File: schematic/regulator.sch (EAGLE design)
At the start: 24 parts, among them J1 COMM, J2 STOP_LIGHT, J3 ON/OFF, J4 IN, J5 DRIVER, Q1 NMOSFETSOT23, Q2 NMOSFETSOT23, Q3 NMOSFETSOT23

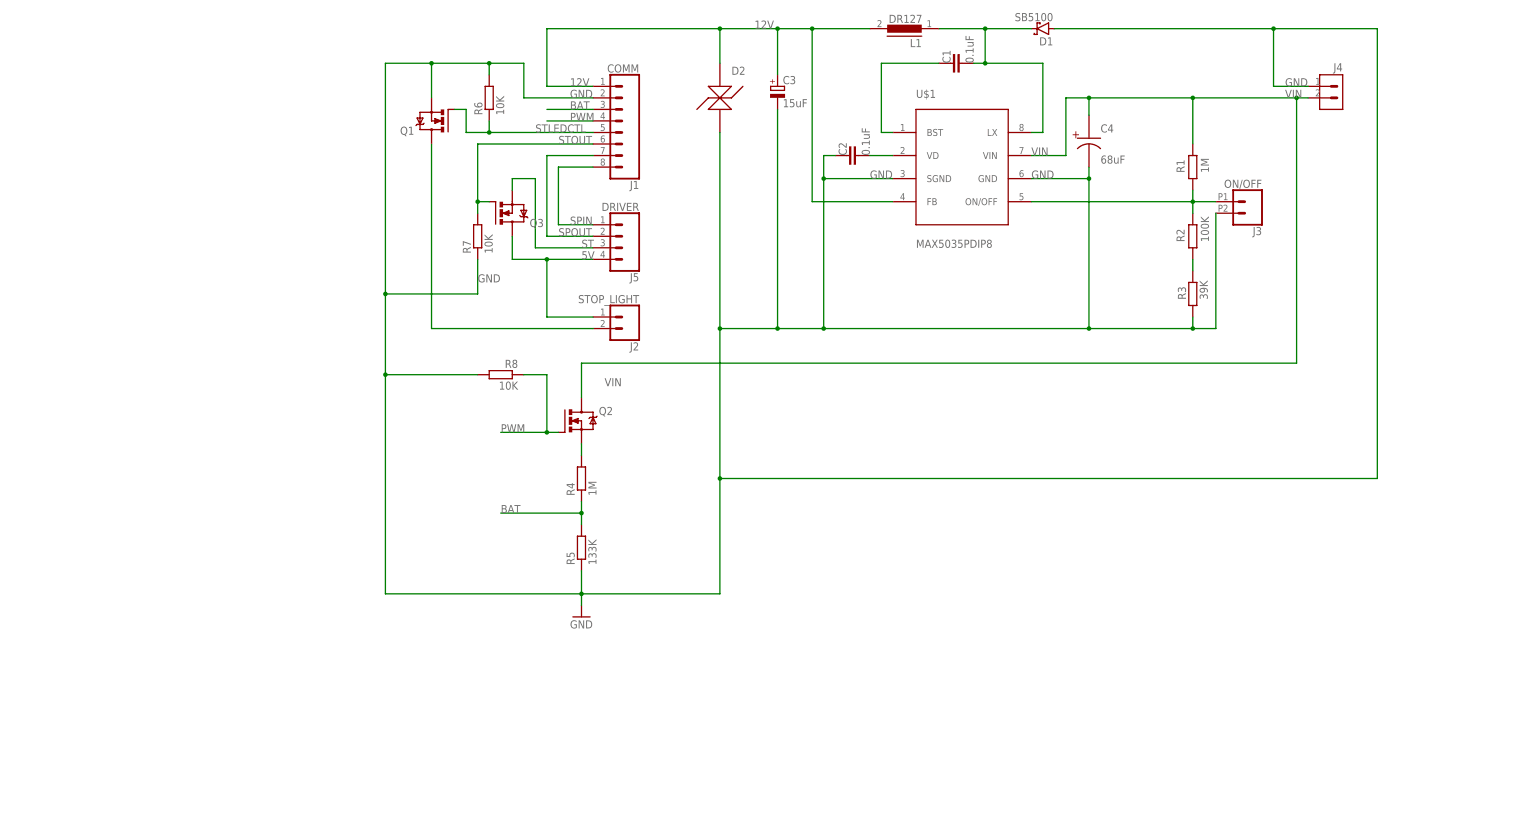
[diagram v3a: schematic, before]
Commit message: Rearrange elements in regulator schematics
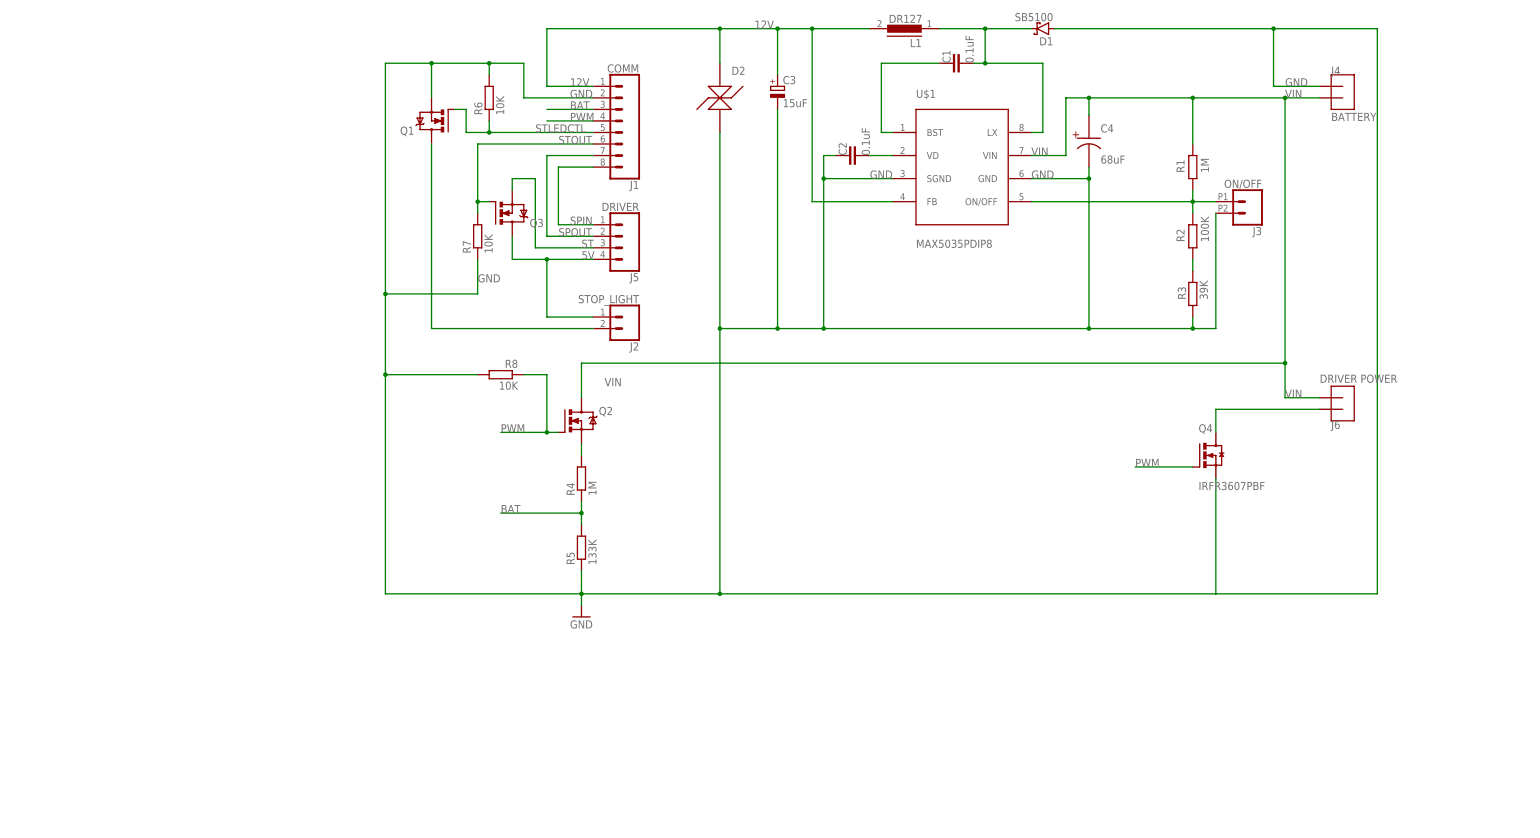
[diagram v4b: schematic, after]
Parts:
- added J6: DRIVER POWER, eScooter:XT60
- added Q4: IRFR3607PBF, Transistor:FQD13N06LTM
- J4: value IN -> BATTERY; device Connectors:B2P-VH(LF)(SN) -> eScooter:XT60
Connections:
- new net P$1: J6.P$1, Q4.D
- net GND: now also J4.P$1, Q4.S; no longer J4.1
- net PWM: now also Q4.G
- net VIN: now also J4.P$2, J6.P$2; no longer J4.2
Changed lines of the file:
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@@
 </classes>
 <parts>
-<part name="J4" library="Connectors" library_urn="urn:adsk.eagle:library:14555660" deviceset="B2P-VH(LF)(SN)" device="" package3d_urn="urn:adsk.eagle:package:10989917/2" value="IN"/>
 <part name="C1" library="Capacitor" library_urn="urn:adsk.eagle:library:16290819" deviceset="C" device="CHIP-1206(3216-METRIC)" package3d_urn="urn:adsk.eagle:package:16290893/2" technology="_" value="0.1uF"/>
 <part name="D1" library="Diodes" library_urn="urn:adsk.eagle:library:11396254" deviceset="MBR360G" device="" package3d_urn="urn:adsk.eagle:package:10898389/2" value="SB5100"/>
@@
 <part name="C4" library="eScooter" deviceset="C" device="PANASONIC_H13" package3d_urn="urn:adsk.eagle:package:21812541/1" value="68uF"/>
 <part name="U$1" library="eScooter" deviceset="MAX5035" device="PDIP8" package3d_urn="urn:adsk.eagle:package:22059831/1"/>
+<part name="J4" library="eScooter" deviceset="XT60" device="" value="BATTERY"/>
+<part name="J6" library="eScooter" deviceset="XT60" device="" value="DRIVER POWER"/>
+<part name="Q4" library="Transistor" library_urn="urn:adsk.eagle:library:14522416" deviceset="FQD13N06LTM" device="" package3d_urn="urn:adsk.eagle:package:10893256/5" value="IRFR3607PBF"/>
 </parts>
 <sheets>
@@
 </plain>
 <instances>
-<instance part="J4" gate="G$1" x="213.36" y="116.84" smashed="yes" rot="MR0">
-<attribute name="NAME" x="215.9" y="122.682" size="1.778" layer="95" rot="MR0"/>
-</instance>
 <instance part="C1" gate="G$1" x="129.54" y="124.46" smashed="yes" rot="R90">
 <attribute name="NAME" x="129.54" y="124.46" size="1.778" layer="95" rot="R90"/>
@@
 <attribute name="NAME" x="121.92" y="116.84" size="1.778" layer="95"/>
 <attribute name="VALUE" x="121.92" y="83.82" size="1.778" layer="96"/>
+</instance>
+<instance part="J4" gate="G$1" x="215.9" y="114.3" smashed="yes">
+<attribute name="NAME" x="213.36" y="121.92" size="1.778" layer="95"/>
+<attribute name="VALUE" x="213.36" y="111.76" size="1.778" layer="96"/>
+</instance>
+<instance part="J6" gate="G$1" x="215.9" y="53.34" smashed="yes" rot="MR180">
+<attribute name="NAME" x="213.36" y="45.72" size="1.778" layer="95" rot="MR180"/>
+<attribute name="VALUE" x="210.82" y="55.88" size="1.778" layer="96" rot="MR180"/>
+</instance>
+<instance part="Q4" gate="G$1" x="185.42" y="38.1" smashed="yes">
+<attribute name="NAME" x="184.15" y="43.18" size="1.778" layer="95"/>
+<attribute name="VALUE" x="184.15" y="30.48" size="1.778" layer="96"/>
 </instance>
 </instances>
@@
 <wire x1="182.88" y1="68.58" x2="182.88" y2="66.04" width="0.1524" layer="91"/>
 <wire x1="182.88" y1="66.04" x2="160.02" y2="66.04" width="0.1524" layer="91"/>
-<pinref part="J4" gate="G$1" pin="1"/>
 <junction x="182.88" y="66.04"/>
 <pinref part="C3" gate="G$1" pin="-"/>
@@
 <junction x="91.44" y="66.04"/>
 <wire x1="48.26" y1="7.62" x2="78.74" y2="7.62" width="0.1524" layer="91"/>
-<wire x1="78.74" y1="7.62" x2="78.74" y2="33.02" width="0.1524" layer="91"/>
 <pinref part="R8" gate="G$1" pin="2"/>
 <wire x1="5.08" y1="55.88" x2="25.4" y2="55.88" width="0.1524" layer="91"/>
@@
 <wire x1="200.66" y1="119.38" x2="200.66" y2="132.08" width="0.1524" layer="91"/>
 <junction x="200.66" y="132.08"/>
-<wire x1="208.28" y1="119.38" x2="200.66" y2="119.38" width="0.1524" layer="91"/>
-<wire x1="223.52" y1="132.08" x2="223.52" y2="33.02" width="0.1524" layer="91"/>
-<wire x1="223.52" y1="33.02" x2="78.74" y2="33.02" width="0.1524" layer="91"/>
+<wire x1="223.52" y1="132.08" x2="223.52" y2="7.62" width="0.1524" layer="91"/>
+<wire x1="223.52" y1="7.62" x2="187.96" y2="7.62" width="0.1524" layer="91"/>
+<wire x1="187.96" y1="7.62" x2="78.74" y2="7.62" width="0.1524" layer="91"/>
 <wire x1="116.84" y1="99.06" x2="101.6" y2="99.06" width="0.1524" layer="91"/>
 <wire x1="101.6" y1="99.06" x2="101.6" y2="104.14" width="0.1524" layer="91"/>
@@
 <junction x="101.6" y="66.04"/>
 <label x="111.76" y="99.06" size="1.778" layer="95"/>
-<wire x1="78.74" y1="66.04" x2="78.74" y2="33.02" width="0.1524" layer="91"/>
+<wire x1="78.74" y1="66.04" x2="78.74" y2="7.62" width="0.1524" layer="91"/>
 <junction x="78.74" y="66.04"/>
-<junction x="78.74" y="33.02"/>
+<junction x="78.74" y="7.62"/>
 <pinref part="C4" gate="G$1" pin="P$2"/>
 <pinref part="U$1" gate="G$1" pin="SGND"/>
 <pinref part="U$1" gate="G$1" pin="GND"/>
+<pinref part="J4" gate="G$1" pin="P$1"/>
+<wire x1="200.66" y1="119.38" x2="210.82" y2="119.38" width="0.1524" layer="91"/>
+<pinref part="Q4" gate="G$1" pin="S"/>
+<wire x1="187.96" y1="33.02" x2="187.96" y2="7.62" width="0.1524" layer="91"/>
 </segment>
 </net>
 <net name="VIN" class="0">
 <segment>
+<pinref part="J6" gate="G$1" pin="P$2"/>
+<wire x1="210.82" y1="50.8" x2="203.2" y2="50.8" width="0.1524" layer="91"/>
+<label x="203.2" y="50.8" size="1.778" layer="95"/>
 <pinref part="Q2" gate="G$1" pin="D"/>
 <wire x1="48.26" y1="50.8" x2="48.26" y2="58.42" width="0.1524" layer="91"/>
@@
 <wire x1="182.88" y1="116.84" x2="182.88" y2="106.68" width="0.1524" layer="91"/>
 <pinref part="R1" gate="G$1" pin="1"/>
-<pinref part="J4" gate="G$1" pin="2"/>
-<wire x1="182.88" y1="116.84" x2="205.74" y2="116.84" width="0.1524" layer="91"/>
+<wire x1="182.88" y1="116.84" x2="203.2" y2="116.84" width="0.1524" layer="91"/>
 <junction x="182.88" y="116.84"/>
-<wire x1="205.74" y1="116.84" x2="208.28" y2="116.84" width="0.1524" layer="91"/>
 <wire x1="154.94" y1="104.14" x2="154.94" y2="116.84" width="0.1524" layer="91"/>
 <wire x1="154.94" y1="116.84" x2="160.02" y2="116.84" width="0.1524" layer="91"/>
@@
 <junction x="160.02" y="116.84"/>
 <label x="203.2" y="116.84" size="1.778" layer="95"/>
-<wire x1="48.26" y1="58.42" x2="205.74" y2="58.42" width="0.1524" layer="91"/>
-<wire x1="205.74" y1="58.42" x2="205.74" y2="116.84" width="0.1524" layer="91"/>
-<junction x="205.74" y="116.84"/>
+<wire x1="48.26" y1="58.42" x2="203.2" y2="58.42" width="0.1524" layer="91"/>
+<wire x1="203.2" y1="58.42" x2="203.2" y2="116.84" width="0.1524" layer="91"/>
+<junction x="203.2" y="116.84"/>
 <pinref part="C4" gate="G$1" pin="P$1"/>
 <label x="147.32" y="104.14" size="1.778" layer="95"/>
 <pinref part="U$1" gate="G$1" pin="VIN"/>
+<pinref part="J4" gate="G$1" pin="P$2"/>
+<wire x1="210.82" y1="116.84" x2="203.2" y2="116.84" width="0.1524" layer="91"/>
+<wire x1="203.2" y1="50.8" x2="203.2" y2="58.42" width="0.1524" layer="91"/>
+<junction x="203.2" y="58.42"/>
 </segment>
 </net>
@@
 <label x="45.72" y="111.76" size="1.778" layer="95"/>
 </segment>
+<segment>
+<pinref part="Q4" gate="G$1" pin="G"/>
+<wire x1="182.88" y1="35.56" x2="170.18" y2="35.56" width="0.1524" layer="91"/>
+<label x="170.18" y="35.56" size="1.778" layer="95"/>
+</segment>
 </net>
 <net name="BAT" class="0">
@@
 </segment>
 </net>
+<net name="P$1" class="0">
+<segment>
+<pinref part="J6" gate="G$1" pin="P$1"/>
+<wire x1="210.82" y1="48.26" x2="187.96" y2="48.26" width="0.1524" layer="91"/>
+<pinref part="Q4" gate="G$1" pin="D"/>
+<wire x1="187.96" y1="48.26" x2="187.96" y2="43.18" width="0.1524" layer="91"/>
+</segment>
+</net>
